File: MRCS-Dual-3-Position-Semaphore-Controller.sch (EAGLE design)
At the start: 21 parts, among them J1 9 VDC, M1 SMALL_SERVO, M2 SMALL_SERVO

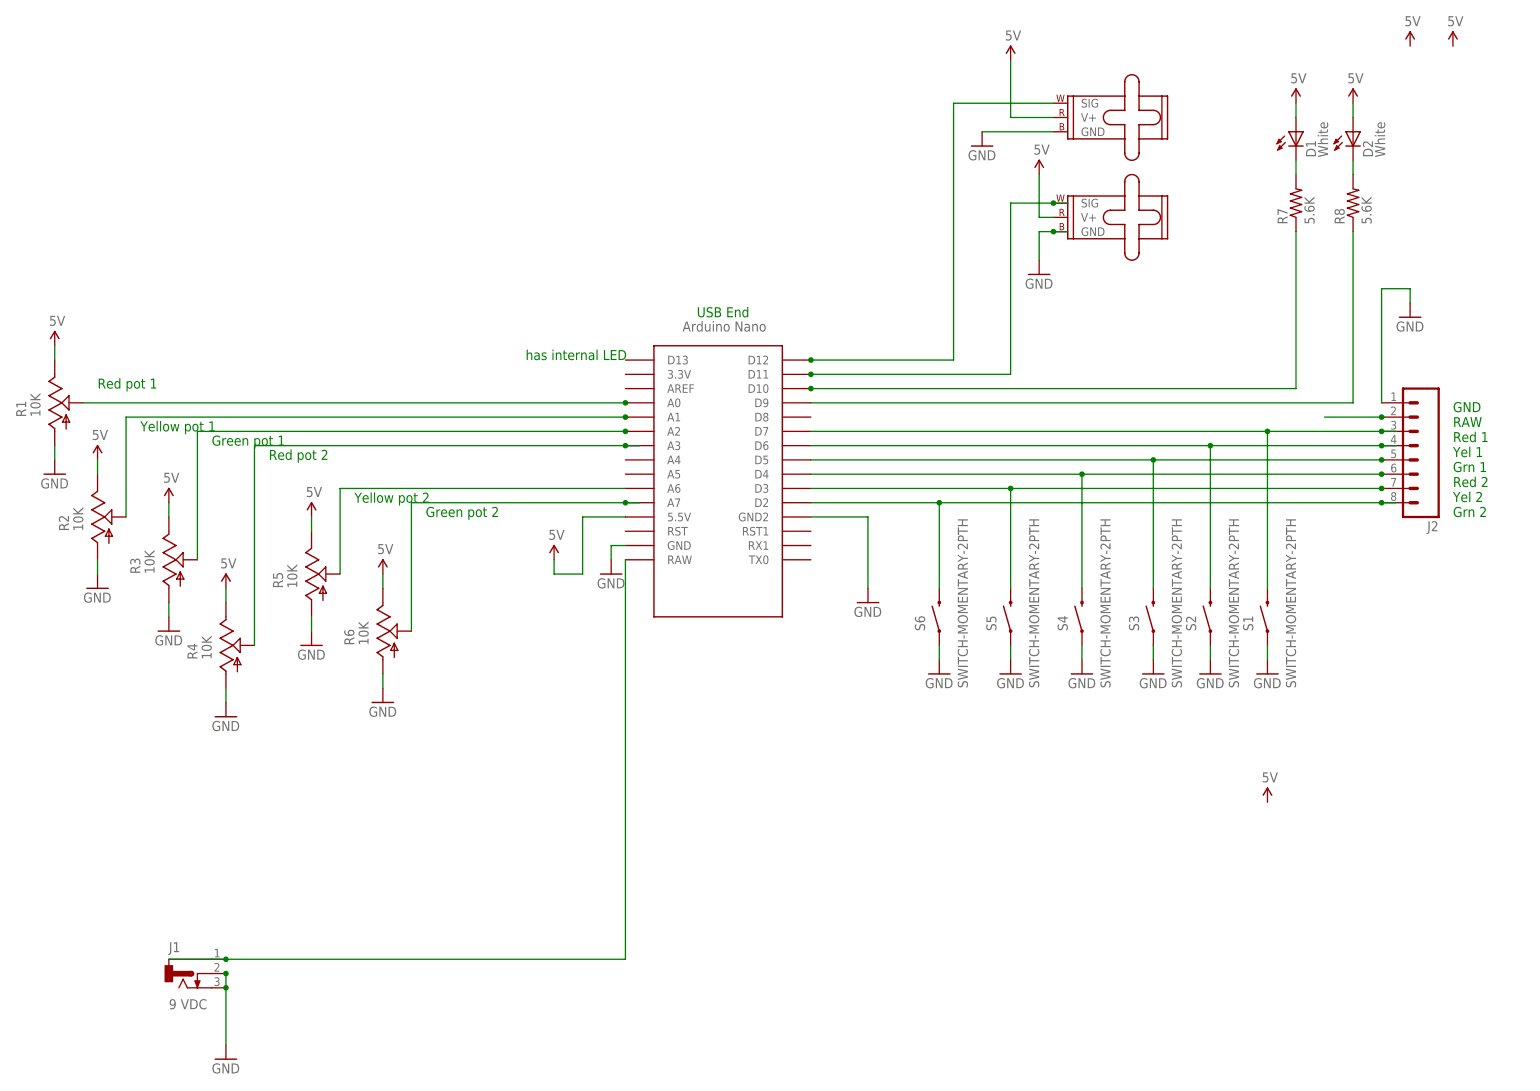
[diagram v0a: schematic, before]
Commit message: Version 1.o documentation package
includes documentation, brd, sch, zip, and sketch
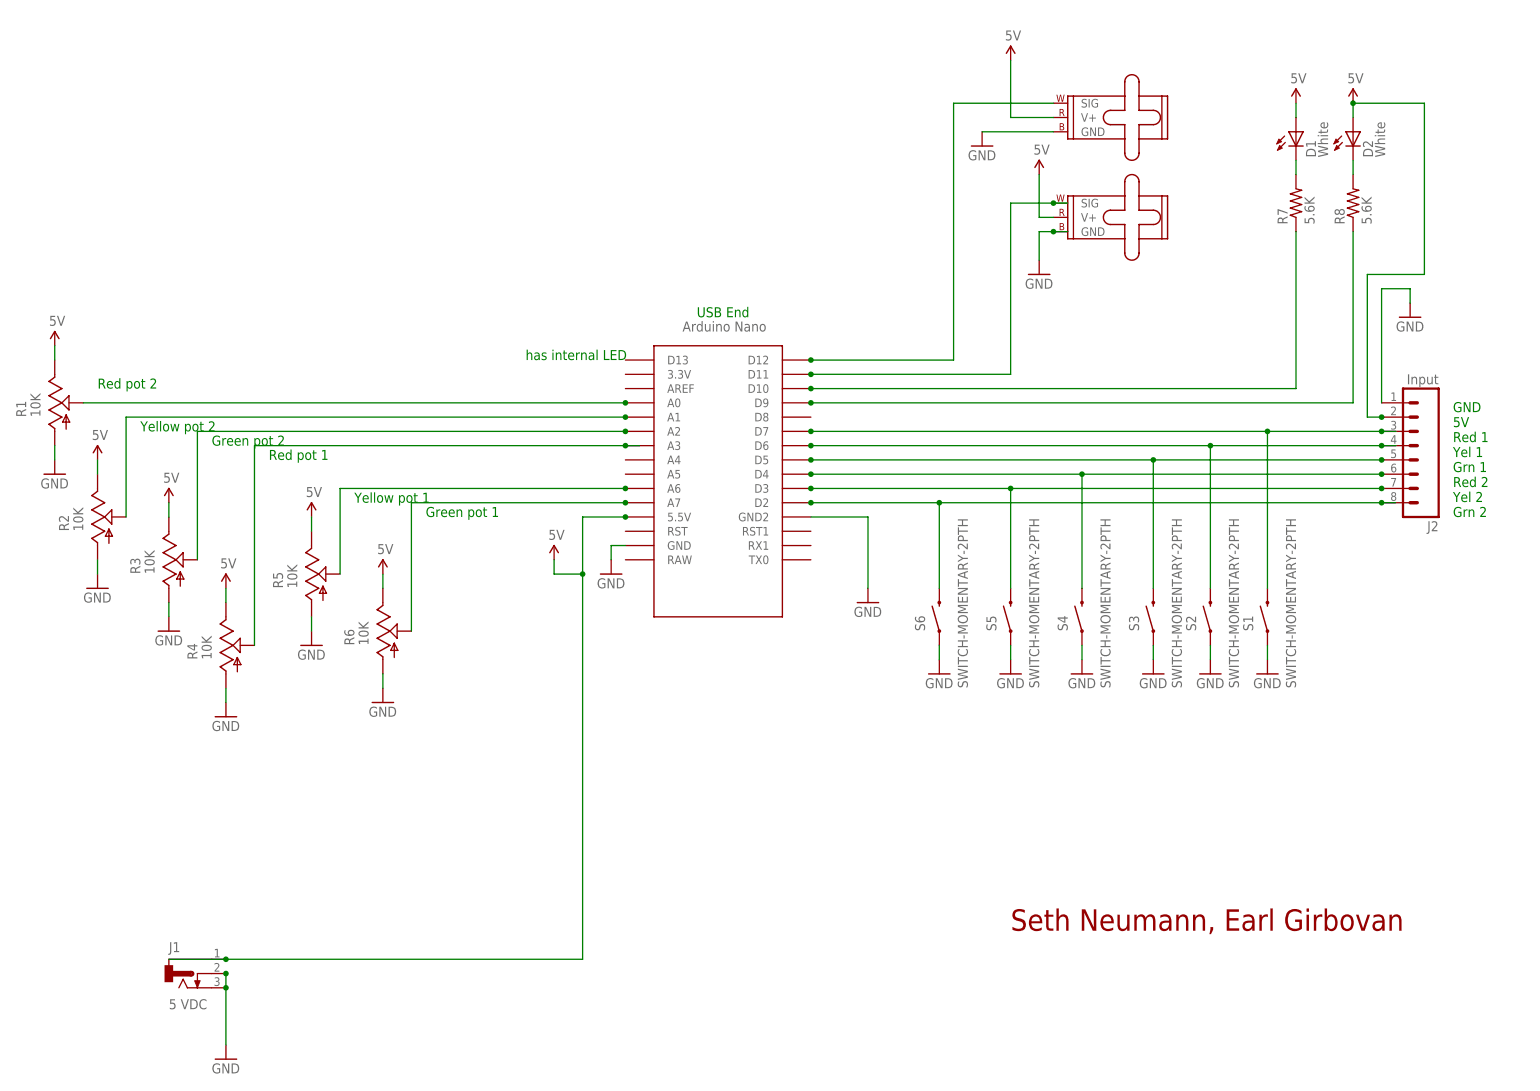
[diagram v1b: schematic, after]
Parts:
- J1: value 9 VDC -> 5 VDC
- J2: value (none) -> Input
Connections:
- net A4 renamed A6
- net A5 renamed A7
- net N$10 renamed D4
- net N$11 renamed D5
- net N$12 renamed D6
- net N$13 renamed D7
- net N$2 renamed D10
- net N$3 renamed D11
- net N$5 renamed D12
- net N$6 renamed D2
- net N$9 renamed D3
- removed net RAW: J1.1, J2.2, NANO.RAW
- net 5V: now also J1.1, J2.2
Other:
- note added: "GND 5V Red 1 Yel 1 Grn 1 Red 2 Yel 2 Grn 2"
- note added: "Seth Neumann, Earl Girbovan"
- note removed: "GND RAW Red 1 Yel 1 Grn 1 Red 2 Yel 2 Grn 2"
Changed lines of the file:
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@@
 </part>
 <part name="NANO" library="Arduino-clone-scn" deviceset="NANO" device=""/>
-<part name="J1" library="SPCoast" deviceset="CONNECTOR-DC-POWER" device="-RA" value="9 VDC"/>
+<part name="J1" library="SPCoast" deviceset="CONNECTOR-DC-POWER" device="-RA" value="5 VDC"/>
 <part name="GND1" library="SparkFun-Aesthetics" deviceset="GND" device=""/>
 <part name="D1" library="SPCoast" deviceset="LED*" device="LED3MM" value="White"/>
@@
 <part name="SUPPLY8" library="SparkFun-Aesthetics" deviceset="5V" device=""/>
 <part name="SUPPLY9" library="SparkFun-Aesthetics" deviceset="5V" device=""/>
-<part name="SUPPLY10" library="SparkFun-Aesthetics" deviceset="5V" device=""/>
 <part name="SUPPLY11" library="SparkFun-Aesthetics" deviceset="5V" device=""/>
 <part name="GND4" library="SparkFun-Aesthetics" deviceset="GND" device=""/>
@@
 <part name="SUPPLY17" library="SparkFun-Aesthetics" deviceset="5V" device=""/>
 <part name="R6" library="MRCS" deviceset="TRIM_US-" device="RS3" value="10K"/>
-<part name="SUPPLY18" library="SparkFun-Aesthetics" deviceset="5V" device=""/>
-<part name="SUPPLY19" library="SparkFun-Aesthetics" deviceset="5V" device=""/>
 <part name="S4" library="SparkFun-Electromechanical" deviceset="SWITCH-MOMENTARY-2" device="PTH"/>
 <part name="GND16" library="SparkFun-Aesthetics" deviceset="GND" device=""/>
@@
 <part name="S1" library="SparkFun-Electromechanical" deviceset="SWITCH-MOMENTARY-2" device="PTH"/>
 <part name="GND20" library="SparkFun-Aesthetics" deviceset="GND" device=""/>
-<part name="J2" library="SPCoast" deviceset="CONNECTOR-M08" device="LOCK"/>
+<part name="J2" library="SPCoast" deviceset="CONNECTOR-M08" device="LOCK" value="Input"/>
 </parts>
 <sheets>
@@
 <plain>
 <text x="71.12" y="119.38" size="1.778" layer="91">has internal LED</text>
-<text x="-5.08" y="114.3" size="1.778" layer="91">Red pot 1</text>
-<text x="2.54" y="106.68" size="1.778" layer="91">Yellow pot 1</text>
-<text x="15.24" y="104.14" size="1.778" layer="91">Green pot 1</text>
-<text x="25.4" y="101.6" size="1.778" layer="91">Red pot 2</text>
-<text x="40.64" y="93.98" size="1.778" layer="91">Yellow pot 2</text>
-<text x="53.34" y="91.44" size="1.778" layer="91">Green pot 2</text>
+<text x="-5.08" y="114.3" size="1.778" layer="91">Red pot 2</text>
+<text x="2.54" y="106.68" size="1.778" layer="91">Yellow pot 2</text>
+<text x="15.24" y="104.14" size="1.778" layer="91">Green pot 2</text>
+<text x="25.4" y="101.6" size="1.778" layer="91">Red pot 1</text>
+<text x="40.64" y="93.98" size="1.778" layer="91">Yellow pot 1</text>
+<text x="53.34" y="91.44" size="1.778" layer="91">Green pot 1</text>
 <text x="236.22" y="91.44" size="1.778" layer="91">GND
-RAW
+5V
 Red 1
 Yel 1
@@
 Grn 2</text>
 <text x="101.6" y="127" size="1.778" layer="91">USB End</text>
+<text x="157.48" y="17.78" size="3.81" layer="94" font="vector">Seth Neumann, Earl Girbovan</text>
 </plain>
 <instances>
-<instance part="FRAME1" gate="G$1" x="-25.4" y="-10.16"/>
+<instance part="FRAME1" gate="G$1" x="-25.4" y="-10.16" smashed="yes"/>
 <instance part="FRAME1" gate="G$2" x="147.32" y="-10.16" smashed="yes">
 <attribute name="LAST_DATE_TIME" x="160.02" y="-8.89" size="2.54" layer="94"/>
@@
 <instance part="SUPPLY8" gate="G$1" x="208.28" y="165.1"/>
 <instance part="SUPPLY9" gate="G$1" x="218.44" y="165.1"/>
-<instance part="SUPPLY10" gate="G$1" x="203.2" y="40.64"/>
 <instance part="SUPPLY11" gate="G$1" x="76.2" y="83.82"/>
 <instance part="GND4" gate="1" x="144.78" y="63.5"/>
@@
 <instance part="SUPPLY17" gate="G$1" x="45.72" y="81.28"/>
 <instance part="R6" gate="G$1" x="45.72" y="71.12"/>
-<instance part="SUPPLY18" gate="G$1" x="236.22" y="175.26"/>
-<instance part="SUPPLY19" gate="G$1" x="228.6" y="175.26"/>
 <instance part="S4" gate="G$1" x="170.18" y="73.66" smashed="yes" rot="R90">
 <attribute name="NAME" x="167.64" y="71.12" size="1.778" layer="95" rot="R90"/>
@@
 </segment>
 </net>
-<net name="RAW" class="0">
-<segment>
-<pinref part="NANO" gate="G$1" pin="RAW"/>
-<wire x1="7.62" y1="12.7" x2="17.78" y2="12.7" width="0.1524" layer="91"/>
-<wire x1="17.78" y1="12.7" x2="88.9" y2="12.7" width="0.3048" layer="91"/>
-<wire x1="88.9" y1="12.7" x2="88.9" y2="83.82" width="0.3048" layer="91"/>
-<pinref part="J1" gate="G$1" pin="1"/>
-<junction x="17.78" y="12.7"/>
-</segment>
-<segment>
-<pinref part="J2" gate="G$1" pin="2"/>
-<wire x1="223.52" y1="109.22" x2="213.36" y2="109.22" width="0.3048" layer="91"/>
-<junction x="223.52" y="109.22"/>
-</segment>
-</net>
 <net name="5V" class="1">
 <segment>
@@
 <pinref part="D2" gate="LED" pin="A"/>
 <wire x1="218.44" y1="162.56" x2="218.44" y2="165.1" width="0.1524" layer="91"/>
+<pinref part="J2" gate="G$1" pin="2"/>
+<wire x1="223.52" y1="109.22" x2="220.98" y2="109.22" width="0.4064" layer="91"/>
+<wire x1="220.98" y1="109.22" x2="220.98" y2="134.62" width="0.4064" layer="91"/>
+<wire x1="220.98" y1="134.62" x2="231.14" y2="134.62" width="0.4064" layer="91"/>
+<wire x1="231.14" y1="134.62" x2="231.14" y2="165.1" width="0.4064" layer="91"/>
+<wire x1="231.14" y1="165.1" x2="218.44" y2="165.1" width="0.4064" layer="91"/>
+<junction x="218.44" y="165.1"/>
+<junction x="223.52" y="109.22"/>
 </segment>
 <segment>
@@
 <pinref part="NANO" gate="G$1" pin="5.5V"/>
 <wire x1="81.28" y1="91.44" x2="88.9" y2="91.44" width="0.3048" layer="91"/>
+<wire x1="7.62" y1="12.7" x2="17.78" y2="12.7" width="0.1524" layer="91"/>
+<pinref part="J1" gate="G$1" pin="1"/>
+<wire x1="17.78" y1="12.7" x2="81.28" y2="12.7" width="0.4064" layer="91"/>
+<wire x1="81.28" y1="12.7" x2="81.28" y2="81.28" width="0.4064" layer="91"/>
+<junction x="81.28" y="81.28"/>
+<junction x="88.9" y="91.44"/>
+<junction x="17.78" y="12.7"/>
 </segment>
 <segment>
@@
 </segment>
 </net>
-<net name="N$2" class="0">
+<net name="D10" class="0">
 <segment>
 <pinref part="NANO" gate="G$1" pin="D10"/>
@@
 </segment>
 </net>
-<net name="N$3" class="0">
+<net name="D11" class="0">
 <segment>
 <pinref part="NANO" gate="G$1" pin="D11"/>
@@
 </segment>
 </net>
-<net name="N$5" class="0">
+<net name="D12" class="0">
 <segment>
 <pinref part="NANO" gate="G$1" pin="D12"/>
@@
 </segment>
 </net>
-<net name="A4" class="0">
+<net name="A6" class="0">
 <segment>
 <wire x1="38.1" y1="81.28" x2="38.1" y2="96.52" width="0.3048" layer="91"/>
@@
 <pinref part="NANO" gate="G$1" pin="A6"/>
 <wire x1="38.1" y1="96.52" x2="88.9" y2="96.52" width="0.3048" layer="91"/>
-</segment>
-</net>
-<net name="A5" class="0">
+<junction x="88.9" y="96.52"/>
+</segment>
+</net>
+<net name="A7" class="0">
 <segment>
 <wire x1="50.8" y1="71.12" x2="50.8" y2="93.98" width="0.3048" layer="91"/>
@@
 <wire x1="50.8" y1="93.98" x2="88.9" y2="93.98" width="0.3048" layer="91"/>
 <pinref part="NANO" gate="G$1" pin="A7"/>
-<wire x1="88.9" y1="93.98" x2="91.44" y2="93.98" width="0.3048" layer="91"/>
 <junction x="88.9" y="93.98"/>
 </segment>
 </net>
-<net name="N$6" class="0">
+<net name="D2" class="0">
 <segment>
 <pinref part="NANO" gate="G$1" pin="D2"/>
@@
 <wire x1="223.52" y1="93.98" x2="226.06" y2="93.98" width="0.3048" layer="91"/>
 <junction x="223.52" y="93.98"/>
-</segment>
-</net>
-<net name="N$9" class="0">
+<junction x="121.92" y="93.98"/>
+</segment>
+</net>
+<net name="D3" class="0">
 <segment>
 <pinref part="NANO" gate="G$1" pin="D3"/>
@@
 <junction x="157.48" y="96.52"/>
 <junction x="223.52" y="96.52"/>
-</segment>
-</net>
-<net name="N$10" class="0">
+<junction x="121.92" y="96.52"/>
+</segment>
+</net>
+<net name="D4" class="0">
 <segment>
 <pinref part="NANO" gate="G$1" pin="D4"/>
@@
 <junction x="170.18" y="99.06"/>
 <junction x="223.52" y="99.06"/>
-</segment>
-</net>
-<net name="N$11" class="0">
+<junction x="121.92" y="99.06"/>
+</segment>
+</net>
+<net name="D5" class="0">
 <segment>
 <pinref part="NANO" gate="G$1" pin="D5"/>
@@
 <junction x="182.88" y="101.6"/>
 <junction x="223.52" y="101.6"/>
-</segment>
-</net>
-<net name="N$12" class="0">
+<junction x="121.92" y="101.6"/>
+</segment>
+</net>
+<net name="D6" class="0">
 <segment>
 <pinref part="NANO" gate="G$1" pin="D6"/>
@@
 <wire x1="223.52" y1="104.14" x2="226.06" y2="104.14" width="0.3048" layer="91"/>
 <junction x="223.52" y="104.14"/>
-</segment>
-</net>
-<net name="N$13" class="0">
+<junction x="121.92" y="104.14"/>
+</segment>
+</net>
+<net name="D7" class="0">
 <segment>
 <pinref part="NANO" gate="G$1" pin="D7"/>
@@
 <wire x1="223.52" y1="106.68" x2="226.06" y2="106.68" width="0.3048" layer="91"/>
 <junction x="223.52" y="106.68"/>
+<junction x="121.92" y="106.68"/>
 </segment>
 </net>
@@
 <pinref part="NANO" gate="G$1" pin="D9"/>
 <wire x1="218.44" y1="111.76" x2="121.92" y2="111.76" width="0.3048" layer="91"/>
-</segment>
-</net>
+<junction x="121.92" y="111.76"/>
+</segment>
+</net>
